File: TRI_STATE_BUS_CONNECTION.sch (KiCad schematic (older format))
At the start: 2 parts

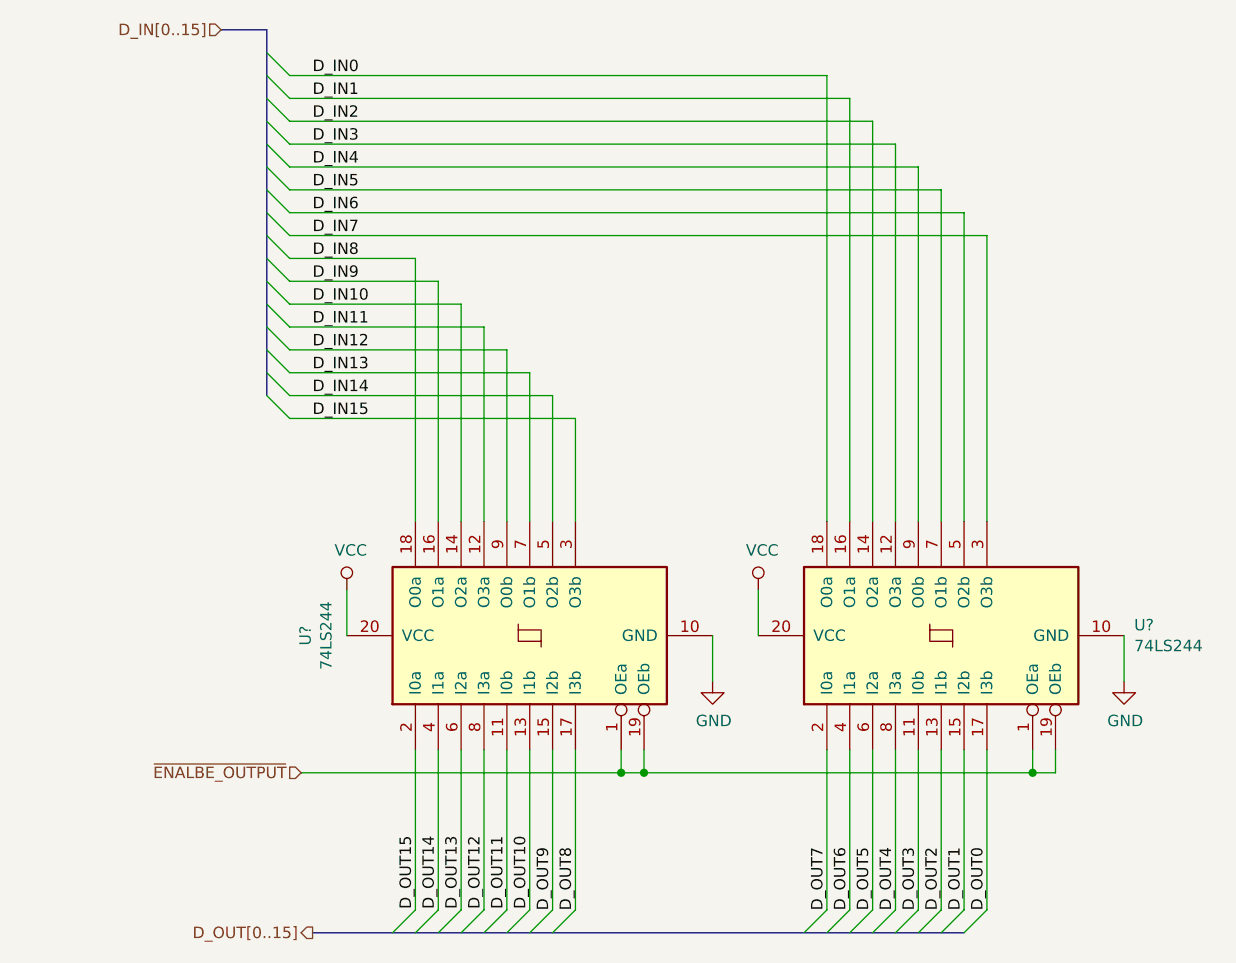
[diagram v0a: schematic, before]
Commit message: alu routed first iteration
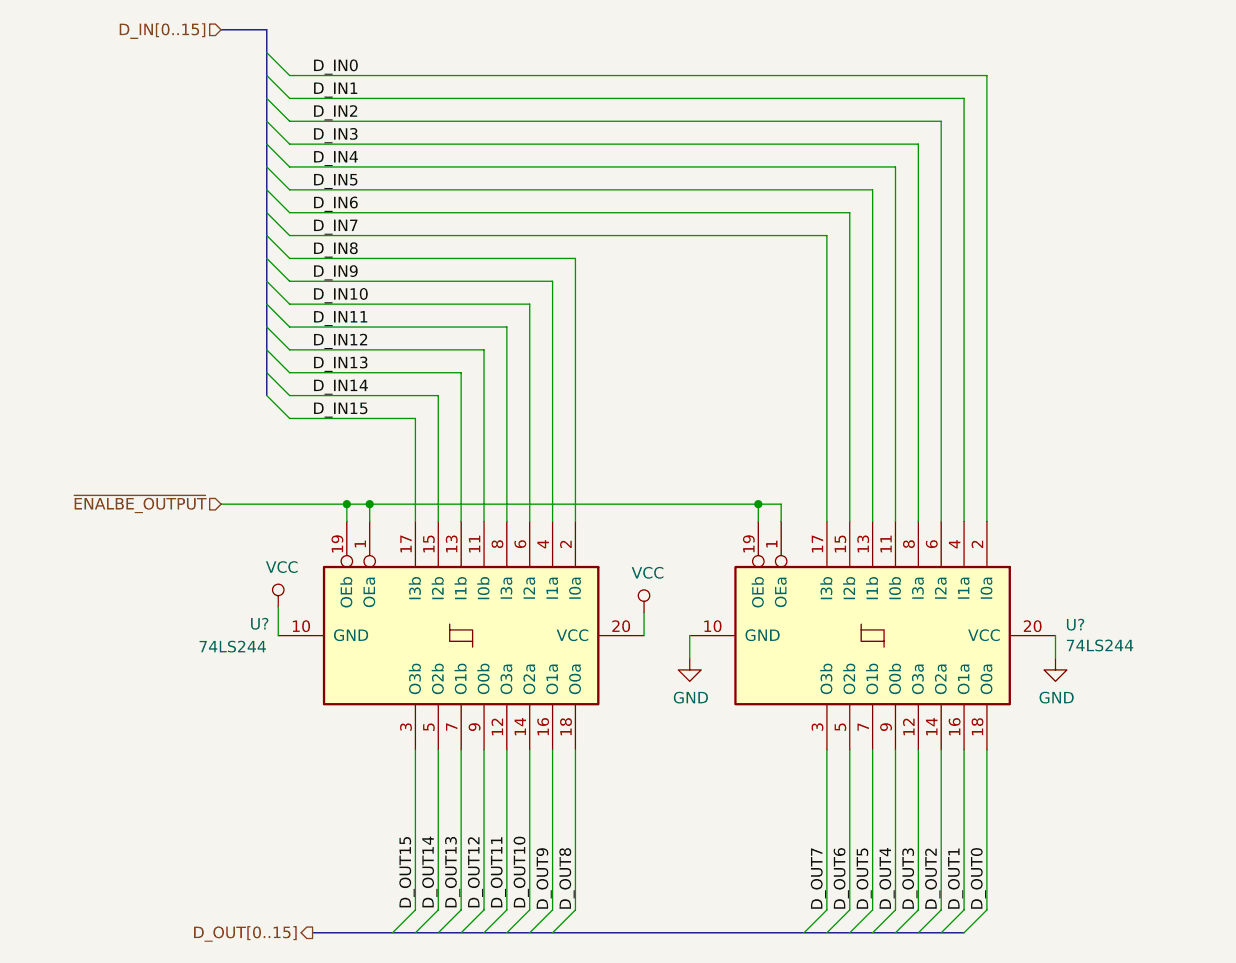
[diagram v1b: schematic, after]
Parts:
- removed U? (x2): 74LS244, symbol 74xx:74LS244
- added U? (x2): 74LS244, symbol 74xx:74LS244
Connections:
- net D_IN0: now also U?.2 (I0a)
- net D_IN1: now also U?.4 (I1a)
- net D_IN10: now also U?.6 (I2a)
- net D_IN11: now also U?.8 (I3a)
- net D_IN12: now also U?.11 (I0b)
- net D_IN13: now also U?.13 (I1b)
- net D_IN14: now also U?.15 (I2b)
- net D_IN15: now also U?.17 (I3b)
- net D_IN2: now also U?.6 (I2a)
- net D_IN3: now also U?.8 (I3a)
- net D_IN4: now also U?.11 (I0b)
- net D_IN5: now also U?.13 (I1b)
- net D_IN6: now also U?.15 (I2b)
- net D_IN7: now also U?.17 (I3b)
- net D_IN8: now also U?.2 (I0a)
- net D_IN9: now also U?.4 (I1a)
- net D_OUT0: now also U?.18 (O0a)
- net D_OUT1: now also U?.16 (O1a)
- net D_OUT10: now also U?.14 (O2a)
- net D_OUT11: now also U?.12 (O3a)
- net D_OUT12: now also U?.9 (O0b)
- net D_OUT13: now also U?.7 (O1b)
- net D_OUT14: now also U?.5 (O2b)
- net D_OUT15: now also U?.3 (O3b)
- net D_OUT2: now also U?.14 (O2a)
- net D_OUT3: now also U?.12 (O3a)
- net D_OUT4: now also U?.9 (O0b)
- net D_OUT5: now also U?.7 (O1b)
- net D_OUT6: now also U?.5 (O2b)
- net D_OUT7: now also U?.3 (O3b)
- net D_OUT8: now also U?.18 (O0a)
- net D_OUT9: now also U?.16 (O1a)
- net GND: now also U?.10 (GND), U?.20 (VCC)
- net VCC: now also U?.10 (GND), U?.20 (VCC)
- net ~ENALBE_OUTPUT~: now also U?.1 (OEa), U?.1 (OEa), U?.19 (OEb), U?.19 (OEb)
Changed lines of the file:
@@
 Comment4 ""
 $EndDescr
-$Comp
-L 74xx:74LS244 U?
-U 1 1 5D39F629
-P 3075 4900
-AR Path="/5D3716A7/5D39F629" Ref="U?"  Part="1"
-AR Path="/5D371796/5D39F629" Ref="U?"  Part="1"
-AR Path="/5D737E0E/5D39F629" Ref="U?"  Part="1"
-AR Path="/5D35BA95/5D39F629" Ref="U?"  Part="1"
-AR Path="/5D35CB6B/5D39F629" Ref="U?"  Part="1"
-AR Path="/5D35D52D/5D399D3F/5D39F629" Ref="U?"  Part="1"
-F 0 "U?" H 3075 5881 50  0000 C CNN
-F 1 "74LS244" H 3075 5790 50  0000 C CNN
-F 2 "" H 3075 4900 50  0001 C CNN
-F 3 "http://www.ti.com/lit/gpn/sn74LS244" H 3075 4900 50  0001 C CNN
-	1    3075 4900
-	0    -1   -1   0
-$EndComp
-$Comp
-L 74xx:74LS244 U?
-U 1 1 5D39F62F
-P 4875 4900
-AR Path="/5D3716A7/5D39F62F" Ref="U?"  Part="1"
-AR Path="/5D371796/5D39F62F" Ref="U?"  Part="1"
-AR Path="/5D737E0E/5D39F62F" Ref="U?"  Part="1"
-AR Path="/5D35BA95/5D39F62F" Ref="U?"  Part="1"
-AR Path="/5D35CB6B/5D39F62F" Ref="U?"  Part="1"
-AR Path="/5D35D52D/5D399D3F/5D39F62F" Ref="U?"  Part="1"
-F 0 "U?" V 4921 4056 50  0000 R CNN
-F 1 "74LS244" V 4830 4056 50  0000 R CNN
-F 2 "" H 4875 4900 50  0001 C CNN
-F 3 "http://www.ti.com/lit/gpn/sn74LS244" H 4875 4900 50  0001 C CNN
-	1    4875 4900
-	0    -1   -1   0
-$EndComp
-Text HLabel 2075 5500 0    50   Input ~ 0
+Text HLabel 1725 4325 0    50   Input ~ 0
 ~ENALBE_OUTPUT~
 Wire Wire Line
-	5075 4400 5075 3150
-Wire Wire Line
-	4975 4400 4975 3050
-Wire Wire Line
-	4875 4400 4875 2950
-Wire Wire Line
-	4775 4400 4775 2850
-Wire Wire Line
-	4675 4400 4675 2750
-Wire Wire Line
-	4575 4400 4575 2650
-Wire Wire Line
-	4475 4400 4475 2550
-Wire Wire Line
-	4375 4400 4375 2450
-Wire Wire Line
-	2025 3350 2675 3350
-Wire Wire Line
-	2025 3650 2975 3650
-Wire Wire Line
-	2025 3750 3075 3750
-Wire Wire Line
-	2025 3950 3275 3950
-Wire Wire Line
-	2025 3250 2575 3250
-Wire Wire Line
-	3275 4400 3275 3950
-Wire Wire Line
-	3175 4400 3175 3850
-Wire Wire Line
-	2025 3850 3175 3850
-Wire Wire Line
-	3075 4400 3075 3750
-Wire Wire Line
-	2975 4400 2975 3650
-Wire Wire Line
-	2875 4400 2875 3550
-Wire Wire Line
-	2025 3550 2875 3550
-Wire Wire Line
-	2775 4400 2775 3450
-Wire Wire Line
-	2025 3450 2775 3450
-Wire Wire Line
-	2675 4400 2675 3350
-Wire Wire Line
-	2575 3250 2575 4400
-Wire Wire Line
-	3475 5400 3475 5500
-Wire Wire Line
-	3475 5500 3575 5500
-Wire Wire Line
-	5375 5500 5375 5400
-Wire Wire Line
-	5275 5400 5275 5500
-Connection ~ 5275 5500
-Wire Wire Line
-	5275 5500 5375 5500
-Wire Wire Line
-	3575 5400 3575 5500
-Connection ~ 3575 5500
+	2025 3850 2675 3850
 $Comp
 L power:GND #PWR?
 U 1 1 5D39F66E
-P 3875 5100
+P 3775 5000
 AR Path="/5D3716A7/5D39F66E" Ref="#PWR?"  Part="1"
 AR Path="/5D371796/5D39F66E" Ref="#PWR?"  Part="1"
@@
 AR Path="/5D35CB6B/5D39F66E" Ref="#PWR?"  Part="1"
 AR Path="/5D35D52D/5D399D3F/5D39F66E" Ref="#PWR?"  Part="1"
-F 0 "#PWR?" H 3875 4850 50  0001 C CNN
-F 1 "GND" H 3880 4927 50  0000 C CNN
-F 2 "" H 3875 5100 50  0001 C CNN
-F 3 "" H 3875 5100 50  0001 C CNN
-	1    3875 5100
+F 0 "#PWR?" H 3775 4750 50  0001 C CNN
+F 1 "GND" H 3780 4827 50  0000 C CNN
+F 2 "" H 3775 5000 50  0001 C CNN
+F 3 "" H 3775 5000 50  0001 C CNN
+	1    3775 5000
 	1    0    0    -1
 $EndComp
-Wire Wire Line
-	3875 4900 3875 5100
 $Comp
 L power:VCC #PWR?
 U 1 1 5D39F675
-P 4075 4700
+P 1975 4775
 AR Path="/5D3716A7/5D39F675" Ref="#PWR?"  Part="1"
 AR Path="/5D371796/5D39F675" Ref="#PWR?"  Part="1"
@@
 AR Path="/5D35CB6B/5D39F675" Ref="#PWR?"  Part="1"
 AR Path="/5D35D52D/5D399D3F/5D39F675" Ref="#PWR?"  Part="1"
-F 0 "#PWR?" H 4075 4550 50  0001 C CNN
-F 1 "VCC" H 4092 4873 50  0000 C CNN
-F 2 "" H 4075 4700 50  0001 C CNN
-F 3 "" H 4075 4700 50  0001 C CNN
-	1    4075 4700
+F 0 "#PWR?" H 1975 4625 50  0001 C CNN
+F 1 "VCC" H 1992 4948 50  0000 C CNN
+F 2 "" H 1975 4775 50  0001 C CNN
+F 3 "" H 1975 4775 50  0001 C CNN
+	1    1975 4775
 	1    0    0    -1
 $EndComp
@@
 L power:VCC #PWR?
 U 1 1 5D39F67B
-P 2275 4700
+P 3575 4800
 AR Path="/5D3716A7/5D39F67B" Ref="#PWR?"  Part="1"
 AR Path="/5D371796/5D39F67B" Ref="#PWR?"  Part="1"
@@
 AR Path="/5D35CB6B/5D39F67B" Ref="#PWR?"  Part="1"
 AR Path="/5D35D52D/5D399D3F/5D39F67B" Ref="#PWR?"  Part="1"
-F 0 "#PWR?" H 2275 4550 50  0001 C CNN
-F 1 "VCC" H 2292 4873 50  0000 C CNN
-F 2 "" H 2275 4700 50  0001 C CNN
-F 3 "" H 2275 4700 50  0001 C CNN
-	1    2275 4700
+F 0 "#PWR?" H 3575 4650 50  0001 C CNN
+F 1 "VCC" H 3592 4973 50  0000 C CNN
+F 2 "" H 3575 4800 50  0001 C CNN
+F 3 "" H 3575 4800 50  0001 C CNN
+	1    3575 4800
 	1    0    0    -1
 $EndComp
-Wire Wire Line
-	2275 4700 2275 4900
-Wire Wire Line
-	4075 4700 4075 4900
-Wire Wire Line
-	2025 2450 4375 2450
-Wire Wire Line
-	2025 2550 4475 2550
-Wire Wire Line
-	2025 2650 4575 2650
-Wire Wire Line
-	2025 2750 4675 2750
-Wire Wire Line
-	2025 2850 4775 2850
-Wire Wire Line
-	2025 2950 4875 2950
-Wire Wire Line
-	2025 3050 4975 3050
-Wire Wire Line
-	2025 3150 5075 3150
 Entry Wire Line
 	2025 2450 1925 2350
@@
 Wire Bus Line
 	1925 2250 1725 2250
-Text Label 2125 2450 0    50   ~ 0
-D_IN0
-Text Label 2125 2550 0    50   ~ 0
-D_IN1
 Text Label 2125 2650 0    50   ~ 0
 D_IN2
@@
 Text Label 2125 3950 0    50   ~ 0
 D_IN15
-Text HLabel 1725 2250 0    50   Input ~ 0
-D_IN[0..15]
-Wire Wire Line
-	3475 5500 2075 5500
-Connection ~ 3475 5500
-Wire Wire Line
-	3575 5500 5275 5500
 Entry Wire Line
 	4975 6100 4875 6200
@@
 	4775 5400 4775 6100
 Wire Wire Line
-	4875 5400 4875 6100
-Wire Wire Line
-	4975 5400 4975 6100
-Wire Wire Line
 	4375 5400 4375 6100
 Wire Wire Line
@@
 Entry Wire Line
 	5075 6100 4975 6200
-Wire Wire Line
-	5075 5400 5075 6100
 Text Label 5075 5825 3    50   ~ 0
 D_OUT0
@@
 Wire Wire Line
 	3175 5400 3175 6100
-Wire Wire Line
-	3075 5400 3075 6100
 Wire Wire Line
 	2975 5400 2975 6100
@@
 L power:GND #PWR?
 U 1 1 5D3A4456
-P 5675 5100
+P 5375 5000
 AR Path="/5D3716A7/5D3A4456" Ref="#PWR?"  Part="1"
 AR Path="/5D371796/5D3A4456" Ref="#PWR?"  Part="1"
@@
 AR Path="/5D35CB6B/5D3A4456" Ref="#PWR?"  Part="1"
 AR Path="/5D35D52D/5D399D3F/5D3A4456" Ref="#PWR?"  Part="1"
-F 0 "#PWR?" H 5675 4850 50  0001 C CNN
-F 1 "GND" H 5680 4927 50  0000 C CNN
-F 2 "" H 5675 5100 50  0001 C CNN
-F 3 "" H 5675 5100 50  0001 C CNN
-	1    5675 5100
+F 0 "#PWR?" H 5375 4750 50  0001 C CNN
+F 1 "GND" H 5380 4827 50  0000 C CNN
+F 2 "" H 5375 5000 50  0001 C CNN
+F 3 "" H 5375 5000 50  0001 C CNN
+	1    5375 5000
 	1    0    0    -1
 $EndComp
-Wire Wire Line
-	5675 5100 5675 4900
 Text Label 2575 5775 3    50   ~ 0
 D_OUT15
 Text HLabel 2125 6200 0    50   Output ~ 0
 D_OUT[0..15]
+Text Label 2125 2550 0    50   ~ 0
+D_IN1
+Text Label 2125 2450 0    50   ~ 0
+D_IN0
+Text HLabel 1725 2250 0    50   Input ~ 0
+D_IN[0..15]
+Wire Wire Line
+	3075 5400 3075 6100
+Wire Wire Line
+	4875 5400 4875 6100
+$Comp
+L 74xx:74LS244 U?
+U 1 1 5EC004DA
+P 4575 4900
+F 0 "U?" V 4529 5744 50  0000 L CNN
+F 1 "74LS244" V 4620 5744 50  0000 L CNN
+F 2 "" H 4575 4900 50  0001 C CNN
+F 3 "http://www.ti.com/lit/gpn/sn74LS244" H 4575 4900 50  0001 C CNN
+	1    4575 4900
+	0    1    1    0
+$EndComp
+Wire Wire Line
+	4975 5400 4975 6100
+Wire Wire Line
+	5075 5400 5075 6100
+$Comp
+L 74xx:74LS244 U?
+U 1 1 5EC03675
+P 2775 4900
+F 0 "U?" V 2725 3975 50  0000 L CNN
+F 1 "74LS244" V 2825 3750 50  0000 L CNN
+F 2 "" H 2775 4900 50  0001 C CNN
+F 3 "http://www.ti.com/lit/gpn/sn74LS244" H 2775 4900 50  0001 C CNN
+	1    2775 4900
+	0    1    1    0
+$EndComp
+Wire Wire Line
+	1975 4900 1975 4775
+Wire Wire Line
+	3575 4900 3575 4800
+Wire Wire Line
+	3775 5000 3775 4900
+Wire Wire Line
+	5375 5000 5375 4900
+Wire Wire Line
+	2025 3950 2575 3950
+Wire Wire Line
+	2575 3950 2575 4400
+Wire Wire Line
+	2675 3850 2675 4400
+Wire Wire Line
+	2025 3750 2775 3750
+Wire Wire Line
+	2775 3750 2775 4400
+Wire Wire Line
+	2025 3650 2875 3650
+Wire Wire Line
+	2875 3650 2875 4400
+Wire Wire Line
+	2975 3550 2975 4400
+Wire Wire Line
+	2025 3550 2975 3550
+Wire Wire Line
+	2025 3450 3075 3450
+Wire Wire Line
+	3075 3450 3075 4400
+Wire Wire Line
+	2025 3350 3175 3350
+Wire Wire Line
+	3175 3350 3175 4400
+Wire Wire Line
+	2025 3250 3275 3250
+Wire Wire Line
+	3275 3250 3275 4400
+Wire Wire Line
+	4375 3150 4375 4400
+Wire Wire Line
+	2025 3150 4375 3150
+Wire Wire Line
+	2025 3050 4475 3050
+Wire Wire Line
+	2025 2950 4575 2950
+Wire Wire Line
+	2025 2850 4675 2850
+Wire Wire Line
+	2025 2750 4775 2750
+Wire Wire Line
+	2025 2650 4875 2650
+Wire Wire Line
+	2025 2550 4975 2550
+Wire Wire Line
+	2025 2450 5075 2450
+Wire Wire Line
+	4475 3050 4475 4400
+Wire Wire Line
+	4575 2950 4575 4400
+Wire Wire Line
+	4675 2850 4675 4400
+Wire Wire Line
+	4775 2750 4775 4400
+Wire Wire Line
+	4875 2650 4875 4400
+Wire Wire Line
+	4975 2550 4975 4400
+Wire Wire Line
+	5075 2450 5075 4400
+Wire Wire Line
+	4175 4400 4175 4325
+Wire Wire Line
+	4175 4325 4075 4325
+Wire Wire Line
+	4075 4325 4075 4400
+Wire Wire Line
+	2375 4400 2375 4325
+Wire Wire Line
+	2275 4325 2275 4400
+Wire Wire Line
+	1725 4325 2275 4325
 Wire Bus Line
 	2125 6200 4975 6200
 Wire Bus Line
 	1925 2250 1925 3850
+Connection ~ 4075 4325
+Connection ~ 2275 4325
+Wire Wire Line
+	2275 4325 2375 4325
+Connection ~ 2375 4325
+Wire Wire Line
+	2375 4325 4075 4325
 $EndSCHEMATC

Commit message: program counter
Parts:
- U? (x2): footprint (none) -> Package_DIP:DIP-20_W7.62mm_LongPads
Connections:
- net GND: now also U?.10 (GND); no longer U?.20 (VCC)
- net VCC: now also U?.20 (VCC); no longer U?.10 (GND)
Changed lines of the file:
@@
 $Descr A4 11693 8268
 encoding utf-8
-Sheet 12 15
+Sheet 5 6
 Title ""
 Date ""
@@
 AR Path="/5D35CB6B/5D39F66E" Ref="#PWR?"  Part="1"
 AR Path="/5D35D52D/5D399D3F/5D39F66E" Ref="#PWR?"  Part="1"
+AR Path="/5EE681E0/5EEF9D6A/5D39F66E" Ref="#PWR017"  Part="1"
 F 0 "#PWR?" H 3775 4750 50  0001 C CNN
 F 1 "GND" H 3780 4827 50  0000 C CNN
@@
 F 3 "" H 3775 5000 50  0001 C CNN
 	1    3775 5000
-	1    0    0    -1
-$EndComp
-$Comp
-L power:VCC #PWR?
-U 1 1 5D39F675
-P 1975 4775
-AR Path="/5D3716A7/5D39F675" Ref="#PWR?"  Part="1"
-AR Path="/5D371796/5D39F675" Ref="#PWR?"  Part="1"
-AR Path="/5D737E0E/5D39F675" Ref="#PWR?"  Part="1"
-AR Path="/5D35BA95/5D39F675" Ref="#PWR?"  Part="1"
-AR Path="/5D35CB6B/5D39F675" Ref="#PWR?"  Part="1"
-AR Path="/5D35D52D/5D399D3F/5D39F675" Ref="#PWR?"  Part="1"
-F 0 "#PWR?" H 1975 4625 50  0001 C CNN
-F 1 "VCC" H 1992 4948 50  0000 C CNN
-F 2 "" H 1975 4775 50  0001 C CNN
-F 3 "" H 1975 4775 50  0001 C CNN
-	1    1975 4775
 	1    0    0    -1
 $EndComp
@@
 AR Path="/5D35CB6B/5D39F67B" Ref="#PWR?"  Part="1"
 AR Path="/5D35D52D/5D399D3F/5D39F67B" Ref="#PWR?"  Part="1"
+AR Path="/5EE681E0/5EEF9D6A/5D39F67B" Ref="#PWR016"  Part="1"
 F 0 "#PWR?" H 3575 4650 50  0001 C CNN
 F 1 "VCC" H 3592 4973 50  0000 C CNN
@@
 Text Label 2675 5775 3    50   ~ 0
 D_OUT14
-$Comp
-L power:GND #PWR?
-U 1 1 5D3A4456
-P 5375 5000
-AR Path="/5D3716A7/5D3A4456" Ref="#PWR?"  Part="1"
-AR Path="/5D371796/5D3A4456" Ref="#PWR?"  Part="1"
-AR Path="/5D737E0E/5D3A4456" Ref="#PWR?"  Part="1"
-AR Path="/5D35BA95/5D3A4456" Ref="#PWR?"  Part="1"
-AR Path="/5D35CB6B/5D3A4456" Ref="#PWR?"  Part="1"
-AR Path="/5D35D52D/5D399D3F/5D3A4456" Ref="#PWR?"  Part="1"
-F 0 "#PWR?" H 5375 4750 50  0001 C CNN
-F 1 "GND" H 5380 4827 50  0000 C CNN
-F 2 "" H 5375 5000 50  0001 C CNN
-F 3 "" H 5375 5000 50  0001 C CNN
-	1    5375 5000
-	1    0    0    -1
-$EndComp
 Text Label 2575 5775 3    50   ~ 0
 D_OUT15
@@
 F 0 "U?" V 4529 5744 50  0000 L CNN
 F 1 "74LS244" V 4620 5744 50  0000 L CNN
-F 2 "" H 4575 4900 50  0001 C CNN
+F 2 "Package_DIP:DIP-20_W7.62mm_LongPads" H 4575 4900 50  0001 C CNN
 F 3 "http://www.ti.com/lit/gpn/sn74LS244" H 4575 4900 50  0001 C CNN
 	1    4575 4900
@@
 Wire Wire Line
 	5075 5400 5075 6100
+Wire Wire Line
+	1975 4900 1975 5025
+Wire Wire Line
+	3575 4900 3575 4800
+Wire Wire Line
+	3775 5000 3775 4900
+Wire Wire Line
+	5375 4775 5375 4900
+Wire Wire Line
+	2025 3950 2575 3950
+Wire Wire Line
+	2575 3950 2575 4400
+Wire Wire Line
+	2675 3850 2675 4400
+Wire Wire Line
+	2025 3750 2775 3750
+Wire Wire Line
+	2775 3750 2775 4400
+Wire Wire Line
+	2025 3650 2875 3650
+Wire Wire Line
+	2875 3650 2875 4400
+Wire Wire Line
+	2975 3550 2975 4400
+Wire Wire Line
+	2025 3550 2975 3550
+Wire Wire Line
+	2025 3450 3075 3450
+Wire Wire Line
+	3075 3450 3075 4400
+Wire Wire Line
+	2025 3350 3175 3350
+Wire Wire Line
+	3175 3350 3175 4400
+Wire Wire Line
+	2025 3250 3275 3250
+Wire Wire Line
+	3275 3250 3275 4400
+Wire Wire Line
+	4375 3150 4375 4400
+Wire Wire Line
+	2025 3150 4375 3150
+Wire Wire Line
+	2025 3050 4475 3050
+Wire Wire Line
+	2025 2950 4575 2950
+Wire Wire Line
+	2025 2850 4675 2850
+Wire Wire Line
+	2025 2750 4775 2750
+Wire Wire Line
+	2025 2650 4875 2650
+Wire Wire Line
+	2025 2550 4975 2550
+Wire Wire Line
+	2025 2450 5075 2450
+Wire Wire Line
+	4475 3050 4475 4400
+Wire Wire Line
+	4575 2950 4575 4400
+Wire Wire Line
+	4675 2850 4675 4400
+Wire Wire Line
+	4775 2750 4775 4400
+Wire Wire Line
+	4875 2650 4875 4400
+Wire Wire Line
+	4975 2550 4975 4400
+Wire Wire Line
+	5075 2450 5075 4400
+Wire Wire Line
+	4175 4400 4175 4325
+Wire Wire Line
+	4175 4325 4075 4325
+Wire Wire Line
+	4075 4325 4075 4400
+Wire Wire Line
+	2375 4400 2375 4325
+Wire Wire Line
+	2275 4325 2275 4400
+Wire Wire Line
+	1725 4325 2275 4325
+Connection ~ 4075 4325
+Connection ~ 2275 4325
+Wire Wire Line
+	2275 4325 2375 4325
+Connection ~ 2375 4325
+Wire Wire Line
+	2375 4325 4075 4325
 $Comp
 L 74xx:74LS244 U?
@@
 F 0 "U?" V 2725 3975 50  0000 L CNN
 F 1 "74LS244" V 2825 3750 50  0000 L CNN
-F 2 "" H 2775 4900 50  0001 C CNN
+F 2 "Package_DIP:DIP-20_W7.62mm_LongPads" H 2775 4900 50  0001 C CNN
 F 3 "http://www.ti.com/lit/gpn/sn74LS244" H 2775 4900 50  0001 C CNN
 	1    2775 4900
 	0    1    1    0
 $EndComp
-Wire Wire Line
-	1975 4900 1975 4775
-Wire Wire Line
-	3575 4900 3575 4800
-Wire Wire Line
-	3775 5000 3775 4900
-Wire Wire Line
-	5375 5000 5375 4900
-Wire Wire Line
-	2025 3950 2575 3950
-Wire Wire Line
-	2575 3950 2575 4400
-Wire Wire Line
-	2675 3850 2675 4400
-Wire Wire Line
-	2025 3750 2775 3750
-Wire Wire Line
-	2775 3750 2775 4400
-Wire Wire Line
-	2025 3650 2875 3650
-Wire Wire Line
-	2875 3650 2875 4400
-Wire Wire Line
-	2975 3550 2975 4400
-Wire Wire Line
-	2025 3550 2975 3550
-Wire Wire Line
-	2025 3450 3075 3450
-Wire Wire Line
-	3075 3450 3075 4400
-Wire Wire Line
-	2025 3350 3175 3350
-Wire Wire Line
-	3175 3350 3175 4400
-Wire Wire Line
-	2025 3250 3275 3250
-Wire Wire Line
-	3275 3250 3275 4400
-Wire Wire Line
-	4375 3150 4375 4400
-Wire Wire Line
-	2025 3150 4375 3150
-Wire Wire Line
-	2025 3050 4475 3050
-Wire Wire Line
-	2025 2950 4575 2950
-Wire Wire Line
-	2025 2850 4675 2850
-Wire Wire Line
-	2025 2750 4775 2750
-Wire Wire Line
-	2025 2650 4875 2650
-Wire Wire Line
-	2025 2550 4975 2550
-Wire Wire Line
-	2025 2450 5075 2450
-Wire Wire Line
-	4475 3050 4475 4400
-Wire Wire Line
-	4575 2950 4575 4400
-Wire Wire Line
-	4675 2850 4675 4400
-Wire Wire Line
-	4775 2750 4775 4400
-Wire Wire Line
-	4875 2650 4875 4400
-Wire Wire Line
-	4975 2550 4975 4400
-Wire Wire Line
-	5075 2450 5075 4400
-Wire Wire Line
-	4175 4400 4175 4325
-Wire Wire Line
-	4175 4325 4075 4325
-Wire Wire Line
-	4075 4325 4075 4400
-Wire Wire Line
-	2375 4400 2375 4325
-Wire Wire Line
-	2275 4325 2275 4400
-Wire Wire Line
-	1725 4325 2275 4325
-Connection ~ 4075 4325
-Connection ~ 2275 4325
-Wire Wire Line
-	2275 4325 2375 4325
-Connection ~ 2375 4325
-Wire Wire Line
-	2375 4325 4075 4325
+$Comp
+L power:GND #PWR?
+U 1 1 5EE83C06
+P 1975 5025
+F 0 "#PWR?" H 1975 4775 50  0001 C CNN
+F 1 "GND" H 1980 4852 50  0000 C CNN
+F 2 "" H 1975 5025 50  0001 C CNN
+F 3 "" H 1975 5025 50  0001 C CNN
+	1    1975 5025
+	1    0    0    -1
+$EndComp
+$Comp
+L power:VCC #PWR?
+U 1 1 5EE85163
+P 5375 4775
+F 0 "#PWR?" H 5375 4625 50  0001 C CNN
+F 1 "VCC" H 5392 4948 50  0000 C CNN
+F 2 "" H 5375 4775 50  0001 C CNN
+F 3 "" H 5375 4775 50  0001 C CNN
+	1    5375 4775
+	1    0    0    -1
+$EndComp
 Wire Bus Line
 	2125 6200 4975 6200
